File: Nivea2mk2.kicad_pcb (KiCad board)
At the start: 2 copper layers, 94 parts, among them J1 Audio-Jack-3, J10 M3, J11 M4, J12 M2, J13 M5, J2 Conn_01x03, J3 Conn_01x03, J4 Jack-DC, J5 SMA, J6 Audio-Jack-3, J7 Conn_01x03, J8 Conn_01x03, J9 M1, Q1 Q_NPN_BEC, Q2 BS170, SW1 SW_Push, U1 4066, U2 TL082, U3 LM386, U4 TL082, U5 74HC240, U6 L78L06_SOT89, Y1 Crystal_GND24

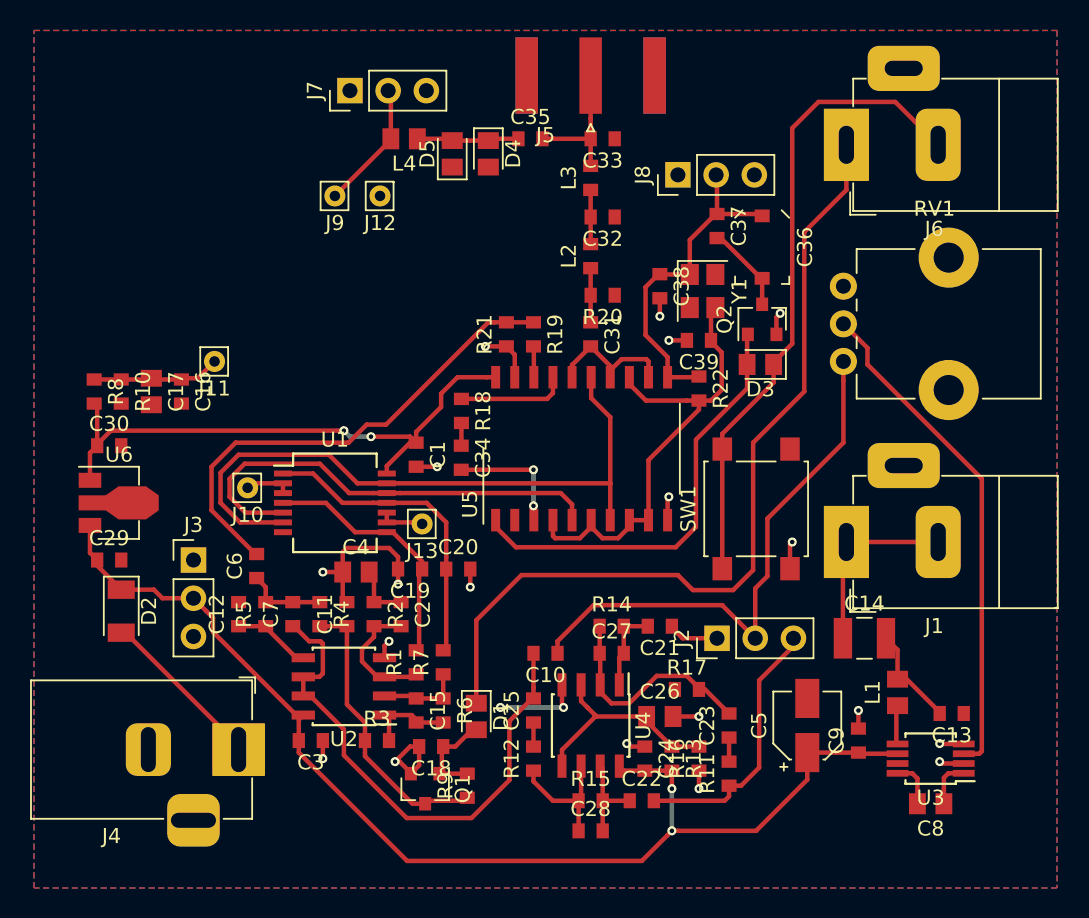
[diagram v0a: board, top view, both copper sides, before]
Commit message: Added edge cuts and picture
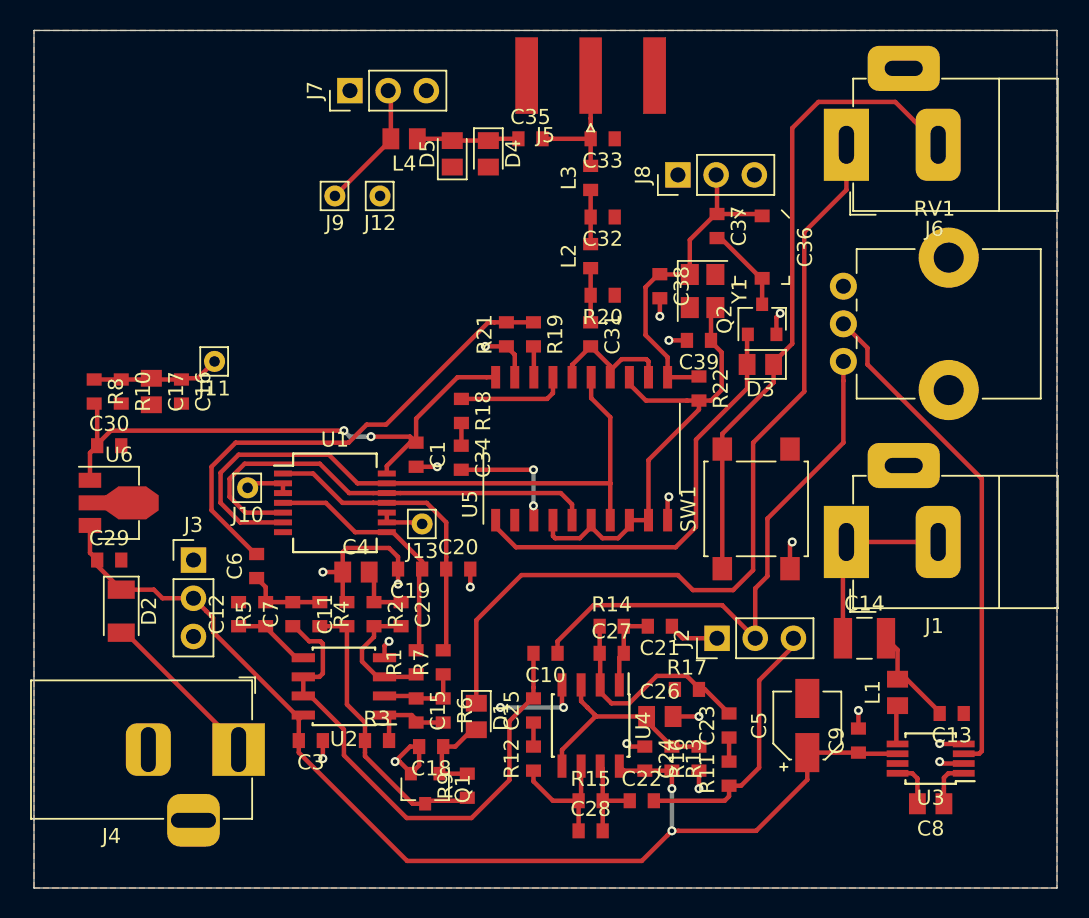
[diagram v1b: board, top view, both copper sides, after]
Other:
- board outline added: 68 x 57 mm
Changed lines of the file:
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@@
   (general
     (thickness 1.6)
-    (drawings 4)
-    (tracks 457)
+    (drawings 8)
+    (tracks 455)
     (zones 0)
     (modules 94)
@@
   )
   (setup
-    (last_trace_width 0.3)
+    (last_trace_width 0.25)
     (user_trace_width 0.3)
     (trace_clearance 0.25)
@@
     )
   )
+  (gr_line (start 122 129) (end 122 72) (layer Edge.Cuts) (width 0.05))
+  (gr_line (start 190 129) (end 122 129) (layer Edge.Cuts) (width 0.05))
+  (gr_line (start 190 72) (end 190 129) (layer Edge.Cuts) (width 0.05))
+  (gr_line (start 122 72) (end 190 72) (layer Edge.Cuts) (width 0.05))
   (dimension 57 (width 0.12) (layer F.SilkS)
     (gr_text "57.000 mm" (at 199.27 100.5 270) (layer F.SilkS)
@@
   (segment (start 147 99) (end 144.4 99) (width 0.3) (layer F.Cu) (net 2))
   (segment (start 147.4 99.4) (end 147 99) (width 0.3) (layer F.Cu) (net 2))
-  (segment (start 152.085 95.05) (end 152.685 95.05) (width 0.3) (layer F.Cu) (net 2))
-  (segment (start 150.15 95.05) (end 152.085 95.05) (width 0.3) (layer F.Cu) (net 2))
-  (segment (start 149.06 96.14) (end 150.15 95.05) (width 0.3) (layer F.Cu) (net 2))
-  (segment (start 149.06 97.03) (end 149.06 96.14) (width 0.3) (layer F.Cu) (net 2))
-  (segment (start 147.4 99.4) (end 147.4 98.69) (width 0.3) (layer F.Cu) (net 2))
-  (segment (start 147.4 98.69) (end 149.06 97.03) (width 0.3) (layer F.Cu) (net 2))
   (segment (start 126.2 97) (end 126 96.8) (width 0.3) (layer F.Cu) (net 2))
   (segment (start 126.2 99.6) (end 126.2 97) (width 0.3) (layer F.Cu) (net 2))
@@
   (segment (start 127.09 98.62) (end 126.2 99.51) (width 0.3) (layer F.Cu) (net 2))
   (segment (start 127.09 98.6) (end 127.09 98.62) (width 0.3) (layer F.Cu) (net 2))
+  (segment (start 152.085 95.05) (end 152.685 95.05) (width 0.3) (layer F.Cu) (net 2))
+  (segment (start 150.15 95.05) (end 152.085 95.05) (width 0.3) (layer F.Cu) (net 2))
+  (segment (start 147.4 99.4) (end 147.4 97.8) (width 0.3) (layer F.Cu) (net 2))
+  (segment (start 147.4 97.8) (end 150.15 95.05) (width 0.3) (layer F.Cu) (net 2))
   (segment (start 146.4 111.6) (end 144.6 111.6) (width 0.3) (layer F.Cu) (net 3))
   (segment (start 147.235 114.965) (end 147.4 114.8) (width 0.3) (layer F.Cu) (net 3))
